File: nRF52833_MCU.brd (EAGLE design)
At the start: 51.3 x 30.2 mm, 64 parts, among them IC1 SKY13415-485LF, J1 282834-2, J100 DEBUG_CONNECTOR, J2 282834-2, J3 282834-2, U1 nRF52833-QIAA, U3 BQ25570RGRR, X1 32MHz, X2 32.768kHz, X3 22-23-2031

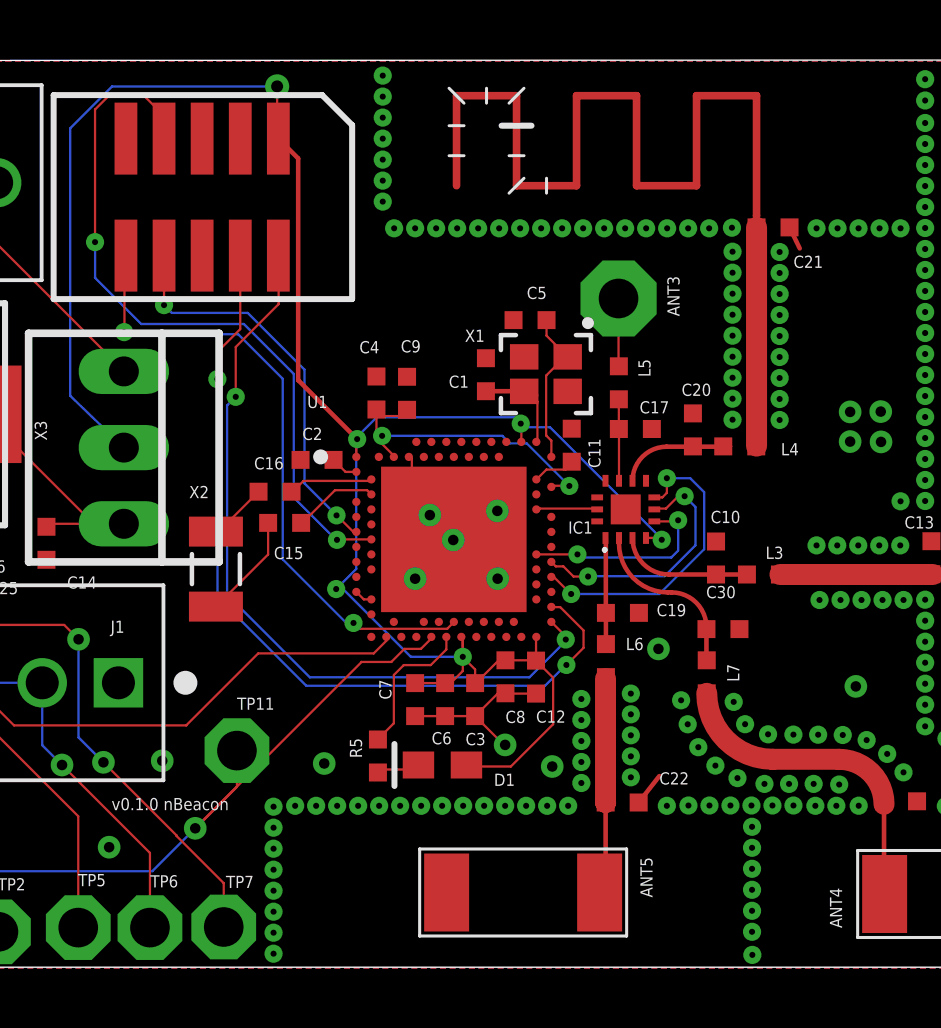
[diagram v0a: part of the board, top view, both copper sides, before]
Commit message: GND via for antenna signal
Signed-off-by: Florian Depraz <florian.depraz@outlook.com>
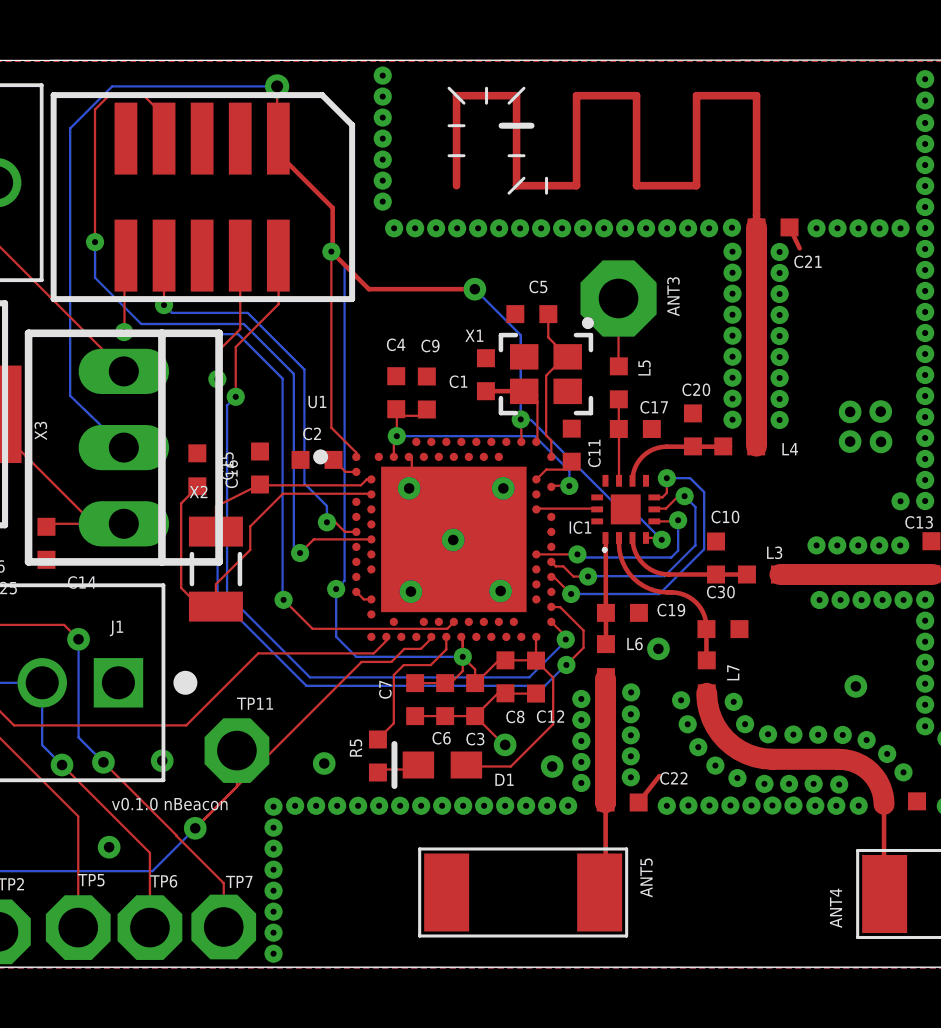
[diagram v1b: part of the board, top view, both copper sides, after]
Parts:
- moved C15 3.41 mm to (24.5, 19.0), turned to 270 degrees
- moved C16 0.93 mm to (26.6, 19.1), turned to 270 degrees
- moved C4 0.66 mm to (31.1, 21.6)
- moved C9 0.66 mm to (32.2, 21.6)
- moved C5 0.21 mm to (35.7, 24.2)
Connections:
- removed net XL1: C16.1, U1.D2
- removed net XL2: C15.1, U1.F2
- net GND: now also C15.1, C16.1
- net N$2: now also U1.D2
- net N$3: now also U1.F2
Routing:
- net VDD: track 70.8 -> 82.5 mm, vias 6 -> 7
- net N$3: track 3.51 -> 12.7 mm
- net N$2: track 1.97 -> 6.28 mm
- net XL1: track 2.98 -> 0.00 mm
- net XL2: track 2.87 -> 0.00 mm
- net P0.07_RX: track 26.2 -> 27.5 mm
- net RESET: track 21.3 -> 22.1 mm
- net N$13: vias 1 -> 0
- net GND: vias 17 -> 93

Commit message: Fix warnings
Signed-off-by: Florian Depraz <florian.depraz@outlook.com>
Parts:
- removed C14, C26, C29: NC, Nordic_misc:RESC0402_N
- removed C23: 0.01uF, Nordic_misc:RESC0402_N
- removed C24, C27: 0.1uF, Nordic_misc:RESC0402_N
- removed C25, C28: 4.7uF, Nordic_misc:RESC0402_N
- removed J1, J2: 282834-2, 282834-2:CONN_282834-2
- removed L1, L2: DR73-220-R, DR73-220-R:DR73
- removed R11: 0.05R, Y14870RXX000B9R:Y14870RXX000B9R
- removed SJ2: (no value), jumper:SJ
- removed TP1, TP11, TP2, TP3, TP4, TP5, TP6, TP7: TPPAD1-13, testpad:P1-13
- removed U3: BQ25570RGRR, BQ25570RGRR:QFN50P350X350X100-21N
- added C18: 1.0pF, Nordic_misc:RESC0402_N
- added C32: 1.2pF, Nordic_misc:RESC0402_N
- added L8: 2.2nH, Nordic_misc:RESC0402_N
- added L9: 4.7nH, Nordic_misc:RESC0402_N
- ANT1, ANT2: value (none) -> 2450AT18B100E; device Nordic_misc:QWMP_MEANDERED_LEFT_+6 -> 2450AT18B100E:ANTC3216X140N
- ANT4, ANT5: value SWRA092B -> 2450AT18B100E; device texas:SWRA092B -> 2450AT18B100E:ANTC3216X140N
- moved X3 38.3 mm to (28.5, 57.5)
- moved ANT5 36.4 mm to (57.3, 33.9), turned to 0 degrees
- moved J3 34.8 mm to (35.3, 57.9)
- moved L4 33.3 mm to (51.5, 51.9), turned to 90 degrees
- moved ANT2 32.6 mm to (50.0, 59.4), turned to 180 degrees
- moved ANT1 32.5 mm to (60.1, 46.1), turned to 90 degrees
- moved C20 31.6 mm to (51.0, 50.3), turned to 180 degrees
- moved L3 31.1 mm to (54.3, 44.6)
- moved C10 31.1 mm to (52.7, 45.2)
- moved X2 30.5 mm to (27.8, 46.1), turned to 0 degrees
- moved IC1 30.4 mm to (47.2, 46.9)
- moved C22 30.3 mm to (47.1, 37.0)
- moved C30 30.3 mm to (50.5, 42.8)
- moved L5 30.3 mm to (47.0, 51.0)
- moved ANT3 30.3 mm to (47.0, 53.8)
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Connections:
- removed net BQ_EXT_VBAT: J1.2, TP6.TP, U3.18
- removed net BQ_LBUCK: L1.2, TP7.TP, U3.16
- removed net BQ_NEN: TP11.TP, U1.AD10, U3.5
- removed net BQ_RSP1: J2.2, R11.P$3, R11.P$4, SJ2.2
- removed net BQ_SUPPLY_VBAT: C14.1, L1.1, X3.3
- removed net BQ_VBAT_OK: U1.AD4, U3.13
- removed net BQ_VBAT_OV: TP2.TP, U3.7
- removed net BQ_VIN_DC: C27.1, C28.1, C29.1, L2.1, R11.P$1, R11.P$2, SJ2.1, U3.2
- removed net BQ_VOUT: U3.14
- removed net BQ_VOUT_EN: TP4.TP, U3.6
- removed net BQ_VOUT_SET: TP5.TP, U3.12
- removed net BQ_VRDIV: U3.8
- removed net BQ_VSTOR: C24.1, C25.1, C26.1, U3.19
- removed net LBOOST: L2.2, U3.20
- removed net N$18: TP1.TP
- removed net VOC_SAMP: TP3.TP, U3.3
- removed net VREF_SAMP: C23.1, U3.4
- new net N$22: IC1.13, L8.2
- new net N$23: C32.1, L8.1, L9.2
- net GND: now also C18.2, C32.2; no longer C14.2, C23.2, C24.2, C25.2, C26.2, C27.2, C28.2, C29.2, J1.1, J2.1, U3.1, U3.10, U3.11, U3.15, U3.17, U3.21, U3.22, U3.23, U3.24, U3.25, U3.9
- net N$13: now also ANT4.1; no longer ANT5.1
- net N$14: now also ANT5.1; no longer ANT4.1
- net N$40: now also ANT2.1; no longer ANT2.P$1
- net N$5: now also ANT1.1; no longer ANT1.P$1
- net NRF_ANT: now also C18.1, L9.1; no longer IC1.13
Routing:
- net BQ_NEN: track 32.4 -> 0.00 mm, vias 2 -> 0
- net BQ_VIN_DC: track 28.6 -> 0.00 mm
- net BQ_LBUCK: track 27.2 -> 0.00 mm, vias 2 -> 0
- net BQ_EXT_VBAT: track 18.8 -> 0.00 mm, vias 2 -> 0
- net BQ_VBAT_OK: track 16.7 -> 0.00 mm
- net GND: track 16.9 -> 3.13 mm, vias 93 -> 39
- net VDD: track 82.5 -> 68.9 mm, vias 7 -> 6
- net VOC_SAMP: track 13.3 -> 0.00 mm
- net P0.07_RX: track 27.5 -> 14.3 mm, vias 2 -> 0
- net BQ_VOUT_SET: track 9.88 -> 0.00 mm
- net ANT_SEL_V3: track 6.69 -> 15.8 mm
- net BQ_SUPPLY_VBAT: track 8.79 -> 0.00 mm
- net ANT_SEL_V2: track 8.40 -> 17.1 mm
- net BQ_RSP1: track 8.45 -> 0.00 mm
- net BQ_VBAT_OV: track 8.41 -> 0.00 mm
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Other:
- board size 51.3 x 30.2 mm -> 47.7 x 30.2 mm
- board text added: "v0.1.1 Beacon"
- board text removed: "v0.1.0 nBeacon"

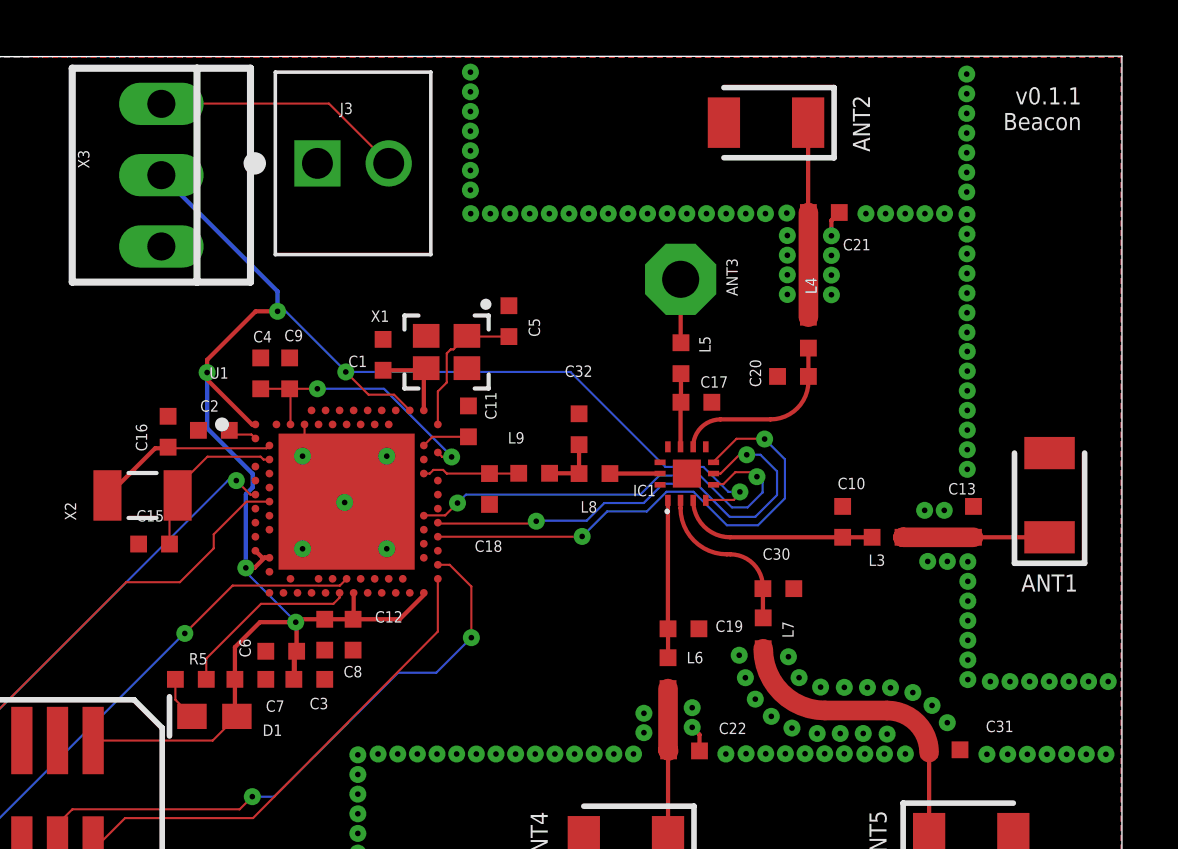
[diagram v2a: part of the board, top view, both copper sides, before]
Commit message: Fix pad/signal spacing issue
Signed-off-by: Florian Depraz <florian.depraz@outlook.com>
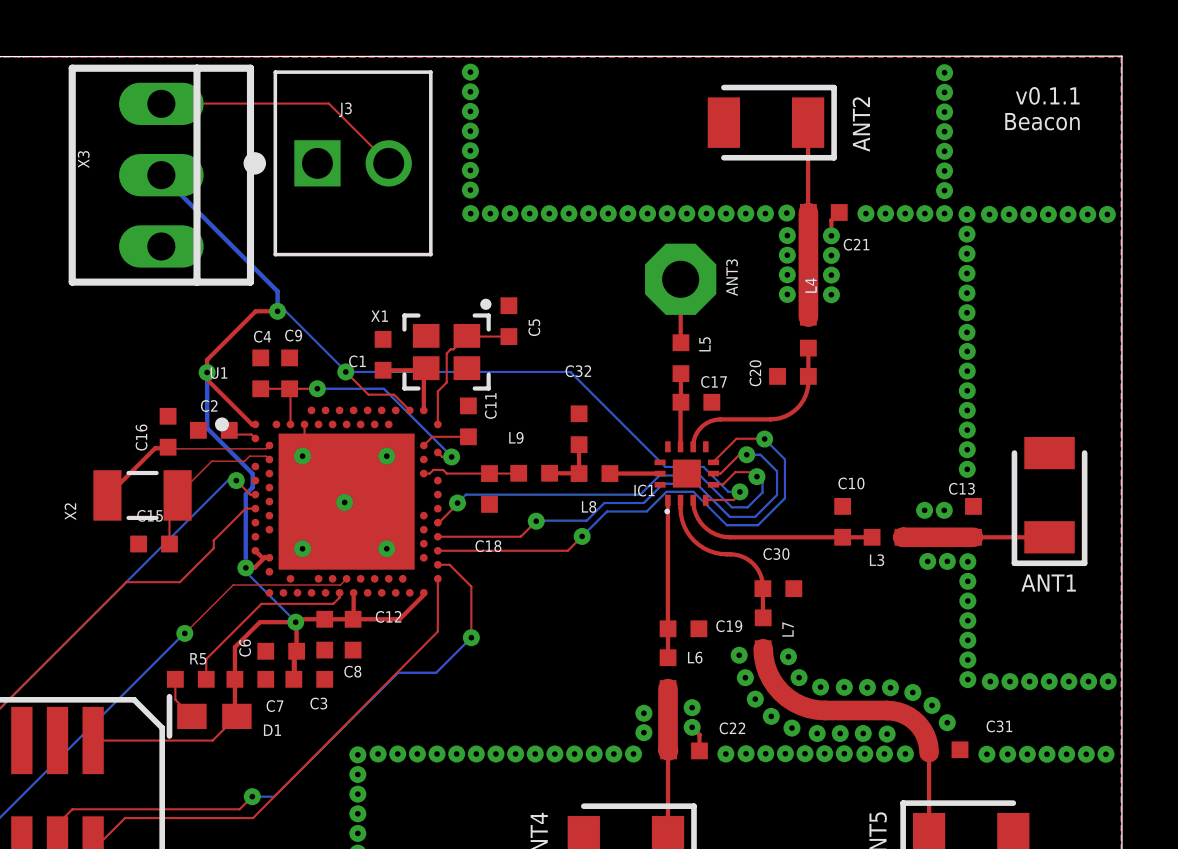
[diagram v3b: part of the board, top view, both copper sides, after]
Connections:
- net ANT_SEL_V1: now also U1.W24; no longer U1.U24
- net ANT_SEL_V2: now also U1.U24; no longer U1.R24
- net ANT_SEL_V3: now also U1.R24; no longer U1.P23
- net P0.07_RX: now also U1.N1; no longer U1.M2
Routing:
- net P0.07_RX: track 14.3 -> 13.6 mm
